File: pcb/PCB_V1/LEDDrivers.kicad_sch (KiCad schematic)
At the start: 50 parts, among them J711 LED +/- (return isolated), J721 LED +/- (return isolated), J731 LED +/- (return isolated), Q711 AOD66923, Q721 AOD66923, U700 SN74LVC1G08DBVR, U710 AL8853S-13, U720 AL8853S-13

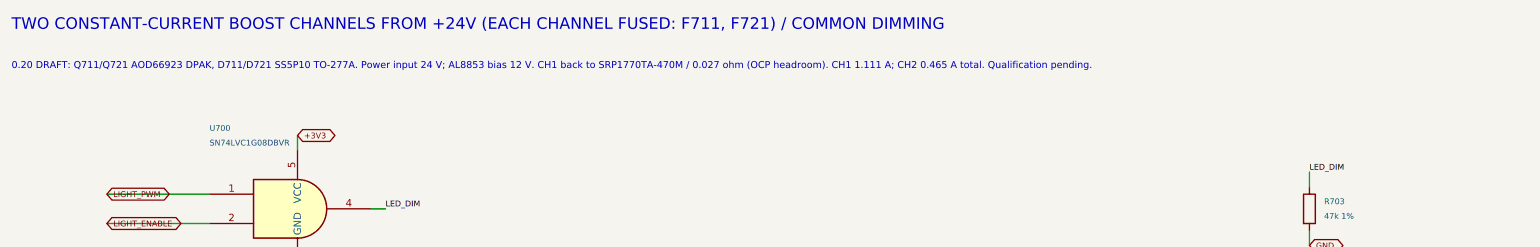
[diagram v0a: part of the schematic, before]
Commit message: pcb: use low-leakage RTC supply diode for revision 0.21
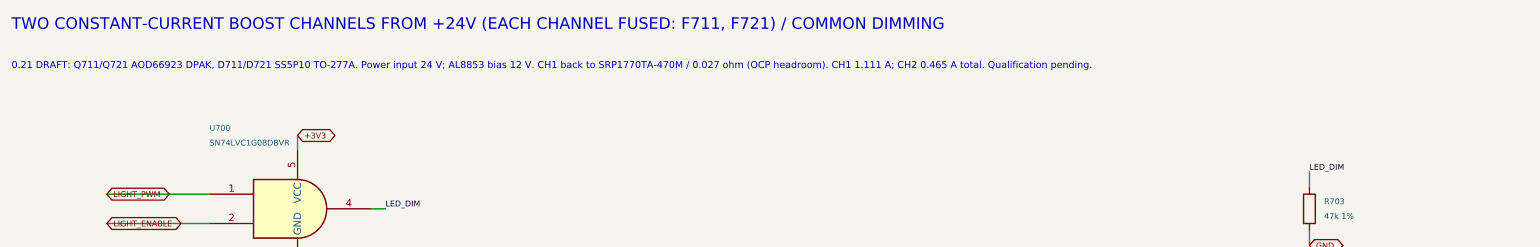
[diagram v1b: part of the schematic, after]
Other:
- note added: "0.21 DRAFT: Q711/Q721 AOD66923 DPAK, D711/D721 SS5P10 TO-277A. Power input 24 V; AL8853 bias 12 V. CH1 back to SRP1770TA-470M / 0.027 ohm (OCP headroom). CH1 1.111 A; CH2 0.465 A total. Qualification pending."
- note removed: "0.20 DRAFT: Q711/Q721 AOD66923 DPAK, D711/D721 SS5P10 TO-277A. Power input 24 V; AL8853 bias 12 V. CH1 back to SRP1770TA-470M / 0.027 ohm (OCP headroom). CH1 1.111 A; CH2 0.465 A total. Qualification pending."
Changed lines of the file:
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@@
 	(title_block
 		(title "07 - AL8853 LED drivers, 24 V input, 2 channels")
-		(date "2026-09-29")
-		(rev "0.20-DRAFT")
+		(date "2026-09-30")
+		(rev "0.21-DRAFT")
 		(company "GrowBox controller")
 		(comment 1 "Simplified prototype; unrouted; hardware qualification pending")
@@
 		)
 	)
-	(text "0.20 DRAFT: Q711/Q721 AOD66923 DPAK, D711/D721 SS5P10 TO-277A. Power input 24 V; AL8853 bias 12 V. CH1 back to SRP1770TA-470M / 0.027 ohm (OCP headroom). CH1 1.111 A; CH2 0.465 A total. Qualification pending."
+	(text "0.21 DRAFT: Q711/Q721 AOD66923 DPAK, D711/D721 SS5P10 TO-277A. Power input 24 V; AL8853 bias 12 V. CH1 back to SRP1770TA-470M / 0.027 ohm (OCP headroom). CH1 1.111 A; CH2 0.465 A total. Qualification pending."
 		(exclude_from_sim no)
 		(at 20.32 22.86 0)
